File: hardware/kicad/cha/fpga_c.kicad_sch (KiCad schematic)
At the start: 28 parts, among them J2 CONF C, U12 iCE40HX4K-TQ144, X1 25 MHz 3,3 V

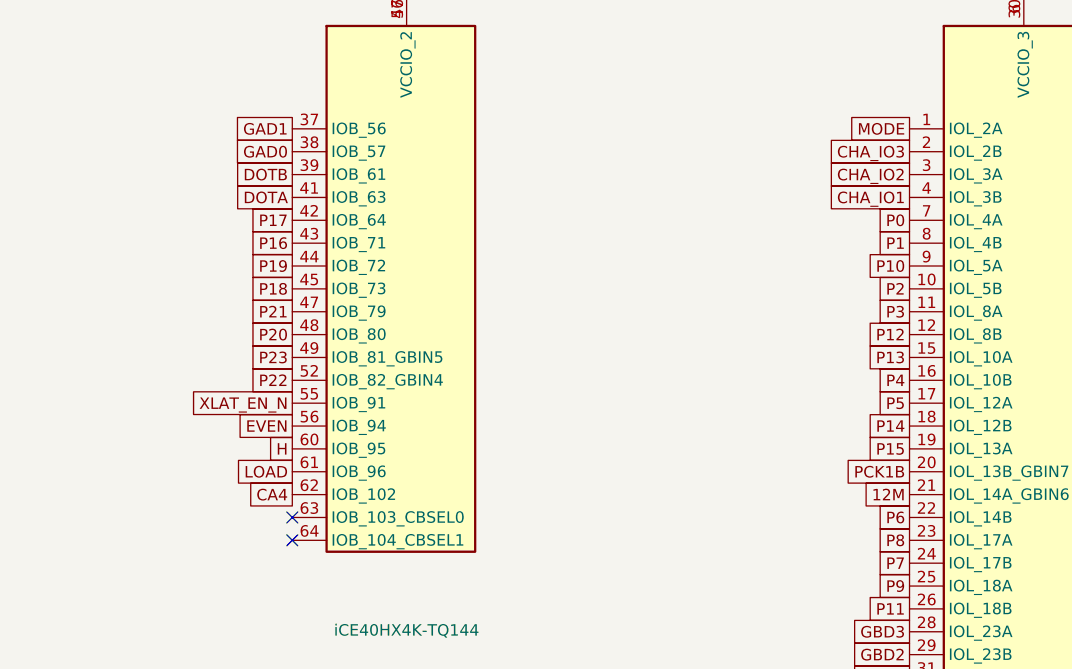
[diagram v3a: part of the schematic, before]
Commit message: CHA : canaux du tampon de sortie U7 groupés par FPGA source
Couche fixe (FPGA SM) puis sprites (FPGA C), chaque groupe dans l'ordre
des contacts : les deux groupes ne se croisent plus le long de la
rangée d'entrée du tampon, où les pistes FIXD enfermaient DOTA et GAD0.
Broches des FPGA C et SM réoptimisées, carte CHA régénérée (contrôle
Freerouting sans violation) ; nouveau routage en cours.

Co-Authored-By: Claude Opus 5.5 <noreply@anthropic.com>
Claude-Session: https://claude.ai/code/session_01WKfXP1YJ8otGxZ5dsY6Agh
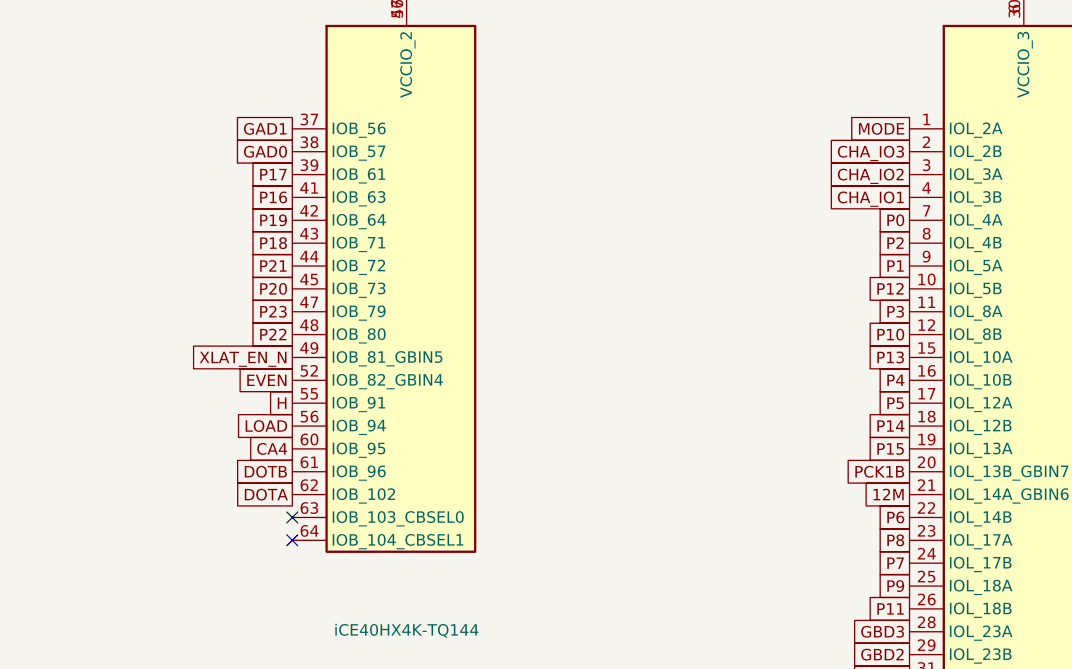
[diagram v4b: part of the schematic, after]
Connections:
- net CA4: now also U12.60 (IOB_95); no longer U12.62 (IOB_102)
- net DOTA: now also U12.62 (IOB_102); no longer U12.41 (IOB_63)
- net DOTB: now also U12.61 (IOB_96); no longer U12.39 (IOB_61)
- net EVEN: now also U12.52 (IOB_82_GBIN4); no longer U12.56 (IOB_94)
- net H: now also U12.55 (IOB_91); no longer U12.60 (IOB_95)
- net LOAD: now also U12.56 (IOB_94); no longer U12.61 (IOB_96)
- net P1: now also U12.9 (IOL_5A); no longer U12.8 (IOL_4B)
- net P10: now also U12.12 (IOL_8B); no longer U12.9 (IOL_5A)
- net P12: now also U12.10 (IOL_5B); no longer U12.12 (IOL_8B)
- net P16: now also U12.41 (IOB_63); no longer U12.43 (IOB_71)
- net P17: now also U12.39 (IOB_61); no longer U12.42 (IOB_64)
- net P18: now also U12.43 (IOB_71); no longer U12.45 (IOB_73)
- net P19: now also U12.42 (IOB_64); no longer U12.44 (IOB_72)
- net P2: now also U12.8 (IOL_4B); no longer U12.10 (IOL_5B)
- net P20: now also U12.45 (IOB_73); no longer U12.48 (IOB_80)
- net P21: now also U12.44 (IOB_72); no longer U12.47 (IOB_79)
- net P22: now also U12.48 (IOB_80); no longer U12.52 (IOB_82_GBIN4)
- net P23: now also U12.47 (IOB_79); no longer U12.49 (IOB_81_GBIN5)
- net XLAT_EN_N: now also U12.49 (IOB_81_GBIN5); no longer U12.55 (IOB_91)

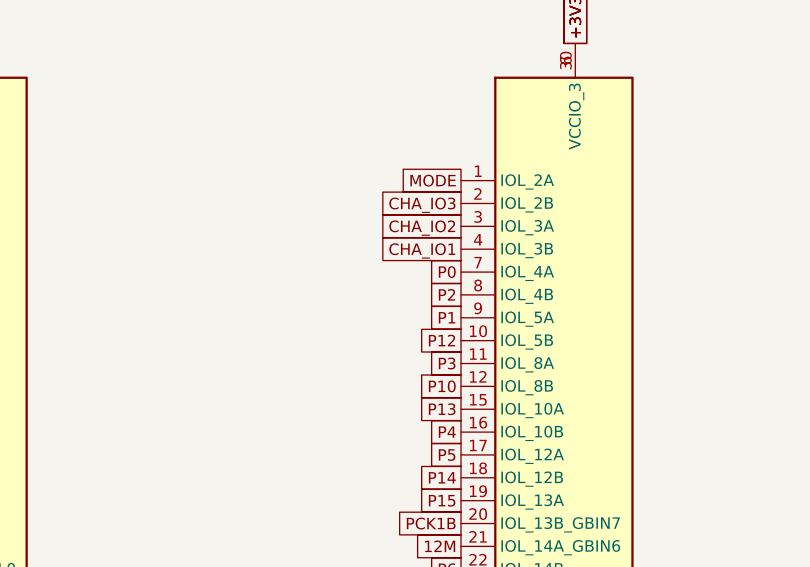
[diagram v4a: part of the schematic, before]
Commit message: Pico 2, microSD et bouton sur la carte PROG ; pistes d'alimentation larges
- La carte PROG est côté avant de la cartouche, composants vers l'avant :
  lecteur microSD et bouton accessibles. Le câble PROG-CHA porte
  désormais le bus de liaison C/SM ; connecteur au même endroit sur les
  deux cartes (x = 172 mm), prêt pour un connecteur carte à carte.
- Sous le Pico : ni piste ni via sur la face composants (pastilles de
  test nues sous le module).
- Classes de réseaux écrites dans le .kicad_pro : +5V et VSYS en 0,5 mm,
  +1V2 en 0,3 mm.
- Broches des FPGA réoptimisées ; contrôle Freerouting sans violation ;
  routage des deux cartes et vérification de timing en cours.

Co-Authored-By: Claude Opus 5.5 <noreply@anthropic.com>
Claude-Session: https://claude.ai/code/session_01WKfXP1YJ8otGxZ5dsY6Agh
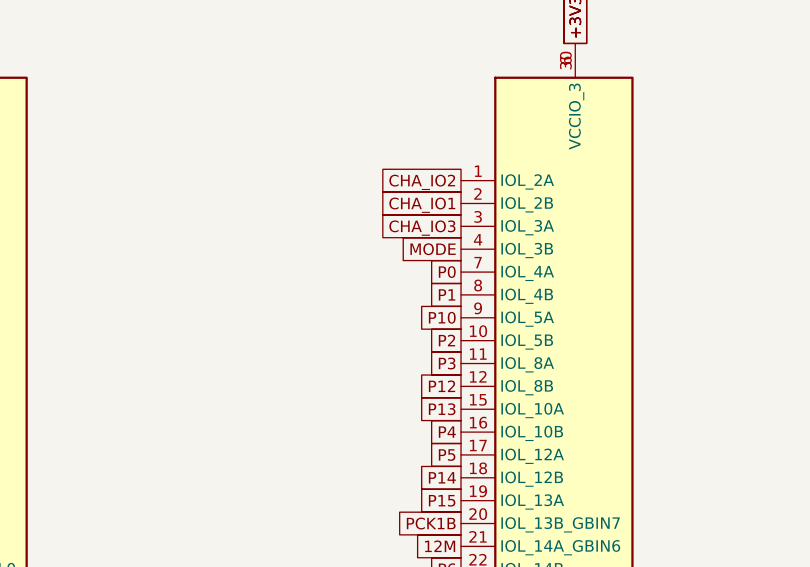
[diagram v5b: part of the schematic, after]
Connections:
- net CHA_IO1: now also U12.2 (IOL_2B); no longer U12.4 (IOL_3B)
- net CHA_IO2: now also U12.1 (IOL_2A); no longer U12.3 (IOL_3A)
- net CHA_IO3: now also U12.3 (IOL_3A); no longer U12.2 (IOL_2B)
- net MODE: now also U12.4 (IOL_3B); no longer U12.1 (IOL_2A)
- net P1: now also U12.8 (IOL_4B); no longer U12.9 (IOL_5A)
- net P10: now also U12.9 (IOL_5A); no longer U12.12 (IOL_8B)
- net P12: now also U12.12 (IOL_8B); no longer U12.10 (IOL_5B)
- net P2: now also U12.10 (IOL_5B); no longer U12.8 (IOL_4B)

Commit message: Régulateur 3,3 V à découpage, horloge SDRAM adaptée côté FPGA, U8 en 74AHCT125
- AP63203 (TSOT-23-6, sortie fixe 3,3 V, ~90 %) à la place de
  l'AMS1117 : ~0,15 W de pertes au lieu de ~0,75 W et moins de courant
  tiré sur le 5 V de la console ; L 4,7 µH, Cin 10 µF, Cout 2 x 22 µF.
- Résistance série de 33 ohms de l'horloge SDRAM déclarée avec le FPGA :
  placée à 2,7 mm de sa broche (au lieu de ~30 mm, côté SDRAM).
- CHA : U8 (16244 pour 2 canaux) remplacé par un 74AHCT125.
Cartes replacées, contrôle Freerouting sans violation ; routage des
deux cartes et vérification de timing en cours.

Co-Authored-By: Claude Opus 5.5 <noreply@anthropic.com>
Claude-Session: https://claude.ai/code/session_01WKfXP1YJ8otGxZ5dsY6Agh
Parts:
- removed C22: 100n, Capacitor_SMD:C_0603_1608Metric, symbol Device:C
- added C42: 100n, Capacitor_SMD:C_0603_1608Metric, symbol Device:C
- added R9: 470, Resistor_SMD:R_0603_1608Metric, symbol Device:R
- C26, C36, C39: value 10u -> 100n; footprint Capacitor_SMD:C_0805_2012Metric -> Capacitor_SMD:C_0603_1608Metric
- C27, C38, C40: value 100n -> 10u; footprint Capacitor_SMD:C_0603_1608Metric -> Capacitor_SMD:C_0805_2012Metric
- R8: value 470 -> 33
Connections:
- net +1V2: now also C27.1
- net +3V3: now also C37.1, C42.1; no longer C27.1, C41.1
- net C_LED: now also U12.81 (IOR_117), R9.1; no longer R8.1, U12.87 (IOR_136)
- net C_LED_K: now also R9.2; no longer R8.2
- net C_SD_CLK: now also R8.1
- net C_VCCPLL0: now also C39.1; no longer C37.1
- net C_VCCPLL1: now also C41.1; no longer C39.1
- net GND: now also C42.2
- net P1: now also U12.9 (IOL_5A); no longer U12.8 (IOL_4B)
- net P10: now also U12.12 (IOL_8B); no longer U12.9 (IOL_5A)
- net P12: now also U12.10 (IOL_5B); no longer U12.12 (IOL_8B)
- net P2: now also U12.8 (IOL_4B); no longer U12.10 (IOL_5B)
- new net C_SD_CLK_R: R8.2

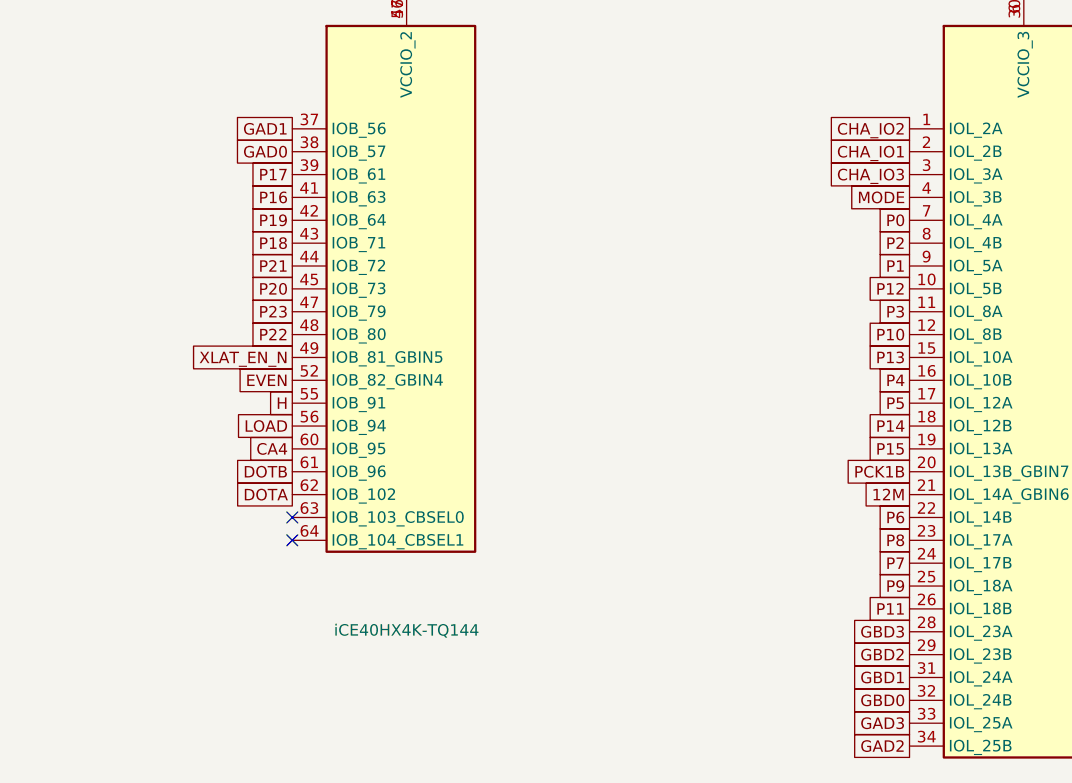
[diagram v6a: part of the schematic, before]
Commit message: CHA : canaux des tampons d'entrée groupés par FPGA de destination
SM seul (bus Z80, PCK2B, 2H1) à gauche, bus P0-P15 au milieu, C seul à
droite, chaque groupe dans l'ordre des contacts : le faisceau SDA entre
le FPGA SM et U3 ne se croise plus avec les signaux du FPGA C (SDA4
restait non routable). Carte CHA replacée, broches réoptimisées,
contrôle Freerouting sans violation ; routage en cours.

Co-Authored-By: Claude Opus 5.5 <noreply@anthropic.com>
Claude-Session: https://claude.ai/code/session_01WKfXP1YJ8otGxZ5dsY6Agh
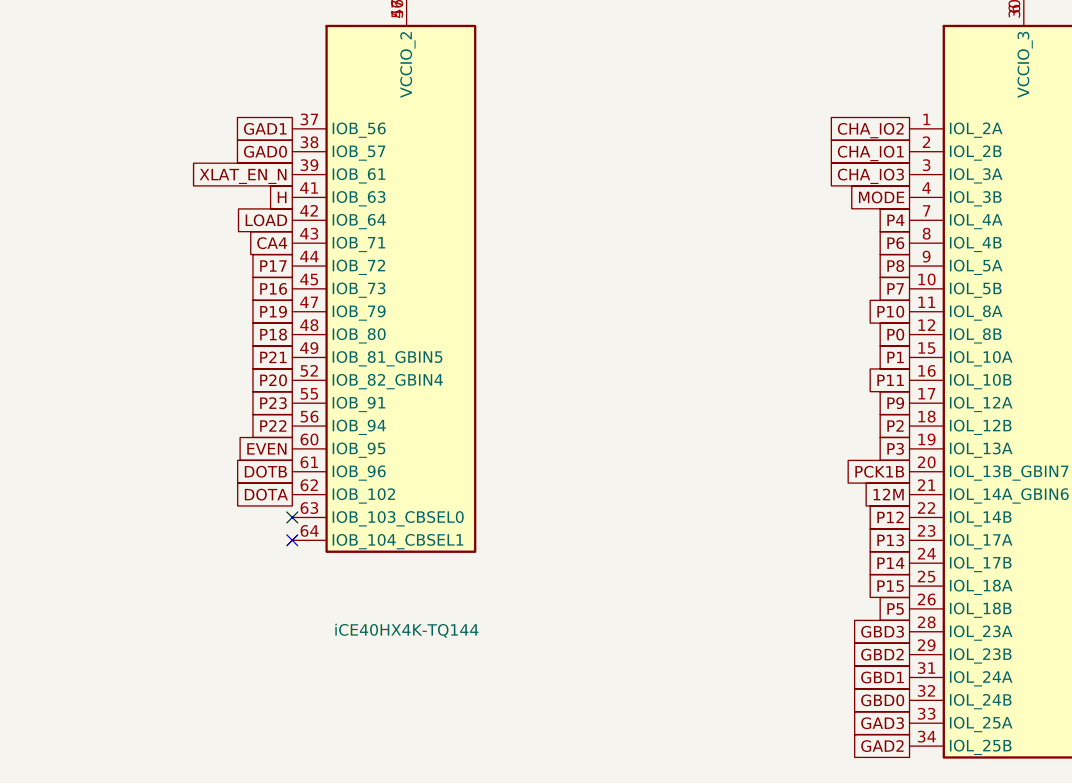
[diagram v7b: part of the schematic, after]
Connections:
- net CA4: now also U12.43 (IOB_71); no longer U12.60 (IOB_95)
- net EVEN: now also U12.60 (IOB_95); no longer U12.52 (IOB_82_GBIN4)
- net H: now also U12.41 (IOB_63); no longer U12.55 (IOB_91)
- net LOAD: now also U12.42 (IOB_64); no longer U12.56 (IOB_94)
- net P0: now also U12.12 (IOL_8B); no longer U12.7 (IOL_4A)
- net P1: now also U12.15 (IOL_10A); no longer U12.9 (IOL_5A)
- net P10: now also U12.11 (IOL_8A); no longer U12.12 (IOL_8B)
- net P11: now also U12.16 (IOL_10B); no longer U12.26 (IOL_18B)
- net P12: now also U12.22 (IOL_14B); no longer U12.10 (IOL_5B)
- net P13: now also U12.23 (IOL_17A); no longer U12.15 (IOL_10A)
- net P14: now also U12.24 (IOL_17B); no longer U12.18 (IOL_12B)
- net P15: now also U12.25 (IOL_18A); no longer U12.19 (IOL_13A)
- net P16: now also U12.45 (IOB_73); no longer U12.41 (IOB_63)
- net P17: now also U12.44 (IOB_72); no longer U12.39 (IOB_61)
- net P18: now also U12.48 (IOB_80); no longer U12.43 (IOB_71)
- net P19: now also U12.47 (IOB_79); no longer U12.42 (IOB_64)
- net P2: now also U12.18 (IOL_12B); no longer U12.8 (IOL_4B)
- net P20: now also U12.52 (IOB_82_GBIN4); no longer U12.45 (IOB_73)
- net P21: now also U12.49 (IOB_81_GBIN5); no longer U12.44 (IOB_72)
- net P22: now also U12.56 (IOB_94); no longer U12.48 (IOB_80)
- net P23: now also U12.55 (IOB_91); no longer U12.47 (IOB_79)
- net P3: now also U12.19 (IOL_13A); no longer U12.11 (IOL_8A)
- net P4: now also U12.7 (IOL_4A); no longer U12.16 (IOL_10B)
- net P5: now also U12.26 (IOL_18B); no longer U12.17 (IOL_12A)
- net P6: now also U12.8 (IOL_4B); no longer U12.22 (IOL_14B)
- net P7: now also U12.10 (IOL_5B); no longer U12.24 (IOL_17B)
- net P8: now also U12.9 (IOL_5A); no longer U12.23 (IOL_17A)
- net P9: now also U12.17 (IOL_12A); no longer U12.25 (IOL_18A)
- net XLAT_EN_N: now also U12.39 (IOB_61); no longer U12.49 (IOB_81_GBIN5)
